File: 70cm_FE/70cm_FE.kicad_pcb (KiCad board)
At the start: 2 copper layers, 67 parts, among them J1 Conn_01x02, J2 U.FL, J3 U.FL, J4 Conn_01x02, J5 U.FL, Q1 BFU520W, U1 HT7533-1, U2 M68710L, U3 74HC14

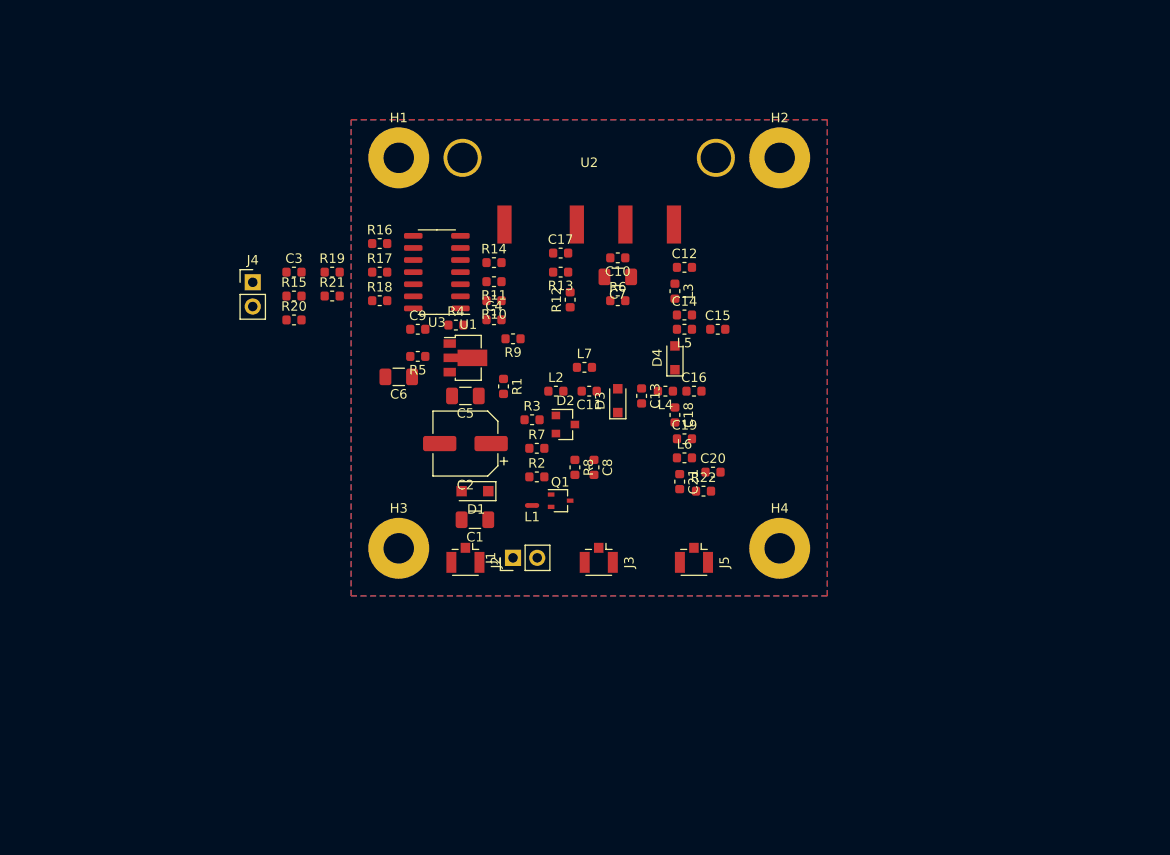
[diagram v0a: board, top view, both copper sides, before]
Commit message: Add some component values, add SAW footprint, change LNA transistor
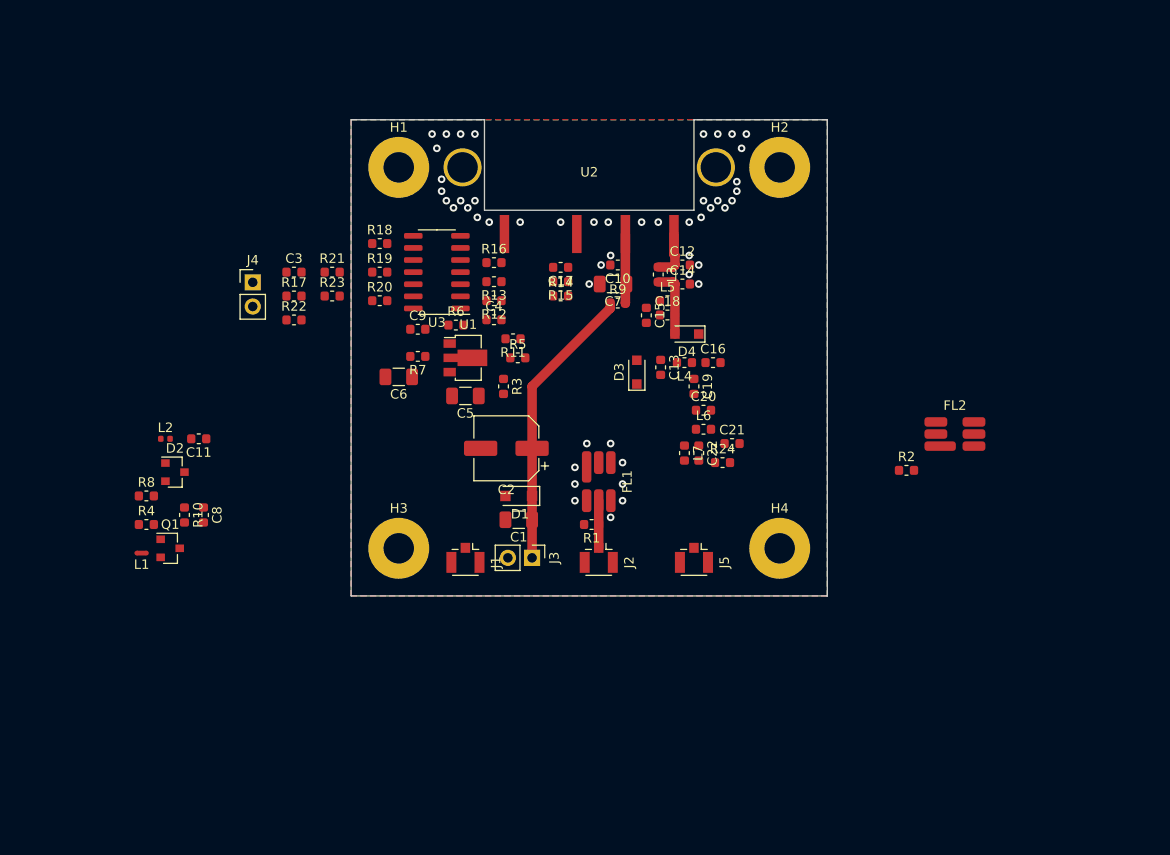
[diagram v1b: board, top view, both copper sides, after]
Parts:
- removed the J1 at (117.0, 96.0)
- removed the R7 at (119.5, 84.5)
- added C18: 2p2, Capacitor_SMD:C_0603_1608Metric, F.Cu at (133.2, 70.5)
- added FL1: AFS434S3, 70cm_FE:AFS434S3, F.Cu at (126.0, 88.0)
- added FL2: AFS434S3, 70cm_FE:AFS434S3, F.Cu at (163.4, 83.0)
- added J3: Conn_01x02, Connector_PinHeader_2.54mm:PinHeader_1x02_P2.54mm_Vertical, F.Cu at (119.0, 96.0)
- added R1: 100k, Resistor_SMD:R_0603_1608Metric, F.Cu at (125.2, 92.5)
- added R10: 2k2, Resistor_SMD:R_0603_1608Metric, F.Cu at (82.5, 91.5)
- added R4: 68, Resistor_SMD:R_0603_1608Metric, F.Cu at (78.5, 92.5)
- C11: value C -> 10p
- C13, C16: value C -> 5p6
- L2: value L -> 15n; footprint Inductor_SMD:L_0603_1608Metric -> Inductor_SMD:L_0402_1005Metric
- L4: value L -> 15n
- L5: value L -> 68n
- Q1: value BFU520W -> 2SC3356; footprint Package_TO_SOT_SMD:SOT-323_SC-70 -> Package_TO_SOT_SMD:SOT-23
- R2: value 68 -> 100k
- R24: renamed from R22; value R -> 100k
- R8: value 1k -> 4k7
- U2: footprint 70cm_pa:M68710L -> 70cm_FE:M68710L
- moved R8 45.1 mm to (78.5, 89.5), turned to 0 degrees
- moved C11 41.3 mm to (84.0, 83.5)
- moved C8 41.3 mm to (84.5, 91.5)
- moved D2 41.3 mm to (81.5, 87.0)
- moved L1 41.3 mm to (78.0, 95.5)
- moved L2 41.3 mm to (80.5, 83.5)
- moved Q1 41.3 mm to (81.0, 95.0)
- moved R2 38.8 mm to (158.3, 86.8)
- moved L7 13.8 mm to (135.0, 85.0), turned to 270 degrees
- moved C15 7.64 mm to (131.0, 70.5), turned to 270 degrees
- moved R5 6.67 mm to (117.5, 75.0)
- moved D1 4.63 mm to (117.6, 89.5)
- moved C1 4.60 mm to (117.6, 92.0)
- moved C2 4.33 mm to (116.3, 84.5)
- moved C13 3.61 mm to (132.5, 76.0)
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- renumbered C18 to C19, C19 to C20, C20 to C21, C21 to C22, J2 to J1, J3 to J2, R9 to R11, R10 to R12, R11 to R13, R12 to R14, R13 to R15, R14 to R16, R15 to R17, R16 to R18, R17 to R19, R18 to R20, R19 to R21, R20 to R22, R21 to R23, R1 to R3, R3 to R5, R4 to R6, R5 to R7, R6 to R9
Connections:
- C3 pad 2: /RX -> Net-(C3-Pad2)
- J1 pad 1: /PA_in -> /TX
- R2 pad 1: /LNA_EN -> Net-(C3-Pad2)
- R2 pad 2: Net-(C3-Pad1) -> GND
- R8 pad 1: Net-(C11-Pad2) -> Net-(Q1-Pad3)
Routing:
- net /V_in: track 0.00 -> 30.2 mm
- net /PA_VDD: track 0.00 -> 7.26 mm
- net Net-(C14-Pad1): track 0.00 -> 7.09 mm
- net /PA_out: track 0.00 -> 5.13 mm
- net /RX: track 0.00 -> 4.95 mm
- net GND: vias 0 -> 50
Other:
- board outline added: 50 x 50 mm

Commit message: Add driver stage and jumpers, clean up schematic
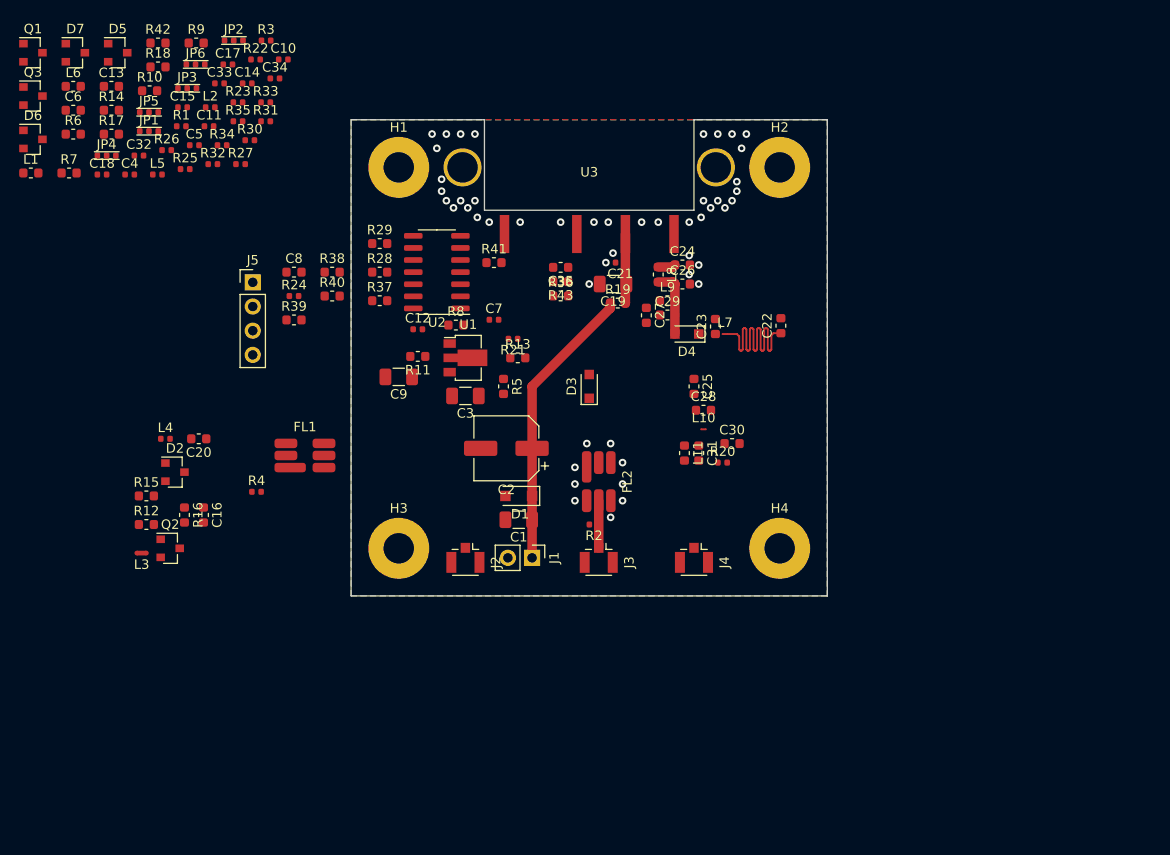
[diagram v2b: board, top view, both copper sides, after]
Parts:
- removed the C3 at (94.0, 66.0)
- removed the J4 at (89.7, 67.1)
- removed the R12 at (115.0, 69.0)
- removed the R13 at (115.0, 67.0)
- removed the R21 at (98.0, 66.0)
- added C10: 10p, Capacitor_SMD:C_0402_1005Metric, F.Cu at (92.9, 43.7)
- added C11: 1n, Capacitor_SMD:C_0402_1005Metric, F.Cu at (85.1, 50.7)
- added C13: 10p, Capacitor_SMD:C_0603_1608Metric, F.Cu at (74.8, 46.5)
- added C14: ?, Capacitor_SMD:C_0402_1005Metric, F.Cu at (89.1, 46.2)
- added C15: 1n, Capacitor_SMD:C_0402_1005Metric, F.Cu at (82.3, 48.7)
- added C17: 1n, Capacitor_SMD:C_0402_1005Metric, F.Cu at (87.1, 44.2)
- added C18: ?, Capacitor_SMD:C_0402_1005Metric, F.Cu at (73.8, 55.8)
- added C32: DNP, Capacitor_SMD:C_0402_1005Metric, F.Cu at (77.7, 53.8)
- added C33: DNP, Capacitor_SMD:C_0402_1005Metric, F.Cu at (86.2, 46.2)
- added C34: DNP, Capacitor_SMD:C_0402_1005Metric, F.Cu at (92.0, 45.7)
- added C4: 1n, Capacitor_SMD:C_0402_1005Metric, F.Cu at (76.8, 55.8)
- added C5: 1n, Capacitor_SMD:C_0402_1005Metric, F.Cu at (83.5, 52.7)
- added C6: 100p, Capacitor_SMD:C_0603_1608Metric, F.Cu at (70.8, 49.0)
- added C8: 100p, Capacitor_SMD:C_0603_1608Metric, F.Cu at (94.0, 66.0)
- added D5: BAV99, Package_TO_SOT_SMD:SOT-23, F.Cu at (75.5, 43.0)
- added D6: BAV99, Package_TO_SOT_SMD:SOT-23, F.Cu at (66.6, 52.1)
- added D7: BAV99, Package_TO_SOT_SMD:SOT-23, F.Cu at (71.0, 43.0)
- added J5: ~, Connector_PinHeader_2.54mm:PinHeader_1x04_P2.54mm_Vertical, F.Cu at (89.7, 67.1)
- added JP1: ~, 70cm_FE:Jumper-3_0402, F.Cu at (78.3, 51.2)
- added JP2: ~, 70cm_FE:Jumper-3_0402, F.Cu at (87.2, 41.7)
- added JP3: ~, 70cm_FE:Jumper-3_0402, F.Cu at (82.3, 46.7)
- added JP4: ~, 70cm_FE:Jumper-3_0402, F.Cu at (73.8, 53.8)
- added JP5: ~, 70cm_FE:Jumper-3_0402, F.Cu at (78.3, 49.2)
- added JP6: ~, 70cm_FE:Jumper-3_0402, F.Cu at (83.2, 44.2)
- added L1: 68n, Inductor_SMD:L_0603_1608Metric, F.Cu at (66.4, 55.6)
- added L2: 15n?, Inductor_SMD:L_0402_1005Metric, F.Cu at (85.2, 48.7)
- added L5: 15n?, Inductor_SMD:L_0402_1005Metric, F.Cu at (79.7, 55.8)
- added L6: 68n, Inductor_SMD:L_0603_1608Metric, F.Cu at (70.8, 46.5)
- added Q1: 2SC3356, Package_TO_SOT_SMD:SOT-23, F.Cu at (66.6, 43.0)
- added Q3: 2SC3356, Package_TO_SOT_SMD:SOT-23, F.Cu at (66.6, 47.5)
- added R1: 100k, Resistor_SMD:R_0402_1005Metric, F.Cu at (82.2, 50.7)
- added R10: 1k, Resistor_SMD:R_0603_1608Metric, F.Cu at (78.8, 47.0)
- added R14: 100, Resistor_SMD:R_0603_1608Metric, F.Cu at (74.8, 49.0)
- added R18: 10, Resistor_SMD:R_0603_1608Metric, F.Cu at (79.7, 44.5)
- added R24: 100k, Resistor_SMD:R_0402_1005Metric, F.Cu at (94.0, 68.5)
- added R25: 0, Resistor_SMD:R_0402_1005Metric, F.Cu at (82.6, 55.2)
- added R26: 0, Resistor_SMD:R_0402_1005Metric, F.Cu at (80.6, 53.2)
- added R27: 0, Resistor_SMD:R_0402_1005Metric, F.Cu at (88.4, 54.7)
- added R3: 100k, Resistor_SMD:R_0402_1005Metric, F.Cu at (91.1, 41.7)
- added R30: DNP, Resistor_SMD:R_0402_1005Metric, F.Cu at (89.4, 52.1)
- added R31: DNP, Resistor_SMD:R_0402_1005Metric, F.Cu at (91.0, 50.2)
- added R32: DNP, Resistor_SMD:R_0402_1005Metric, F.Cu at (85.5, 54.7)
- added R33: DNP, Resistor_SMD:R_0402_1005Metric, F.Cu at (91.0, 48.2)
- added R34: DNP, Resistor_SMD:R_0402_1005Metric, F.Cu at (86.5, 52.7)
- added R35: DNP, Resistor_SMD:R_0402_1005Metric, F.Cu at (88.1, 50.2)
- added R38: DNP, Resistor_SMD:R_0603_1608Metric, F.Cu at (98.0, 66.0)
- added R39: 0, Resistor_SMD:R_0603_1608Metric, F.Cu at (94.0, 71.0)
- added R40: DNP, Resistor_SMD:R_0603_1608Metric, F.Cu at (98.0, 68.5)
- added R42: 100, Resistor_SMD:R_0603_1608Metric, F.Cu at (79.7, 41.9)
- added R6: 1, Resistor_SMD:R_0603_1608Metric, F.Cu at (70.8, 51.5)
- added R7: 4k7, Resistor_SMD:R_0603_1608Metric, F.Cu at (70.4, 55.6)
- added R9: 1k, Resistor_SMD:R_0603_1608Metric, F.Cu at (83.7, 41.9)
- C12: renamed from C9; footprint Capacitor_SMD:C_0603_1608Metric -> Capacitor_SMD:C_0402_1005Metric
- C21: renamed from C10; footprint Capacitor_SMD:C_0603_1608Metric -> Capacitor_SMD:C_0402_1005Metric
- C7: renamed from C4; value 100n -> 1n; footprint Capacitor_SMD:C_0603_1608Metric -> Capacitor_SMD:C_0402_1005Metric
- J1: renamed from J3; value Conn_01x02 -> ~
- L10: renamed from L6; footprint Inductor_SMD:L_0603_1608Metric -> 70cm_FE:NetTie-2_SMD_Pad0.2mm
- L7: renamed from L4; footprint Inductor_SMD:L_0603_1608Metric -> 70cm_FE:NetTie-2_SMD_Pad0.2mm
- R17: value 100k -> 1
- R2: renamed from R1; footprint Resistor_SMD:R_0603_1608Metric -> Resistor_SMD:R_0402_1005Metric
- R20: renamed from R24; footprint Resistor_SMD:R_0603_1608Metric -> Resistor_SMD:R_0402_1005Metric
- R21: renamed from R11; footprint Resistor_SMD:R_0603_1608Metric -> Resistor_SMD:R_0402_1005Metric
- R22: footprint Resistor_SMD:R_0603_1608Metric -> Resistor_SMD:R_0402_1005Metric
- R23: value DNP -> 0; footprint Resistor_SMD:R_0603_1608Metric -> Resistor_SMD:R_0402_1005Metric
- R28: renamed from R19; value 1k -> 100
- R29: renamed from R18; value 0 -> 100k
- R4: renamed from R2; footprint Resistor_SMD:R_0603_1608Metric -> Resistor_SMD:R_0402_1005Metric
- moved FL1 68.3 mm to (95.2, 85.2)
- moved R4 68.3 mm to (90.1, 89.1)
- moved R22 27.6 mm to (90.0, 43.7)
- moved R17 25.6 mm to (74.8, 51.5)
- moved R23 22.6 mm to (88.1, 48.2)
- moved C22 13.4 mm to (145.1, 71.6), turned to 90 degrees
- moved D3 5.22 mm to (125.0, 78.0)
- moved L7 5.20 mm to (139.2, 72.5), turned to 0 degrees
- moved C23 3.80 mm to (138.2, 71.7), turned to 90 degrees
- moved C21 0.35 mm to (128.2, 65.0)
- moved R2 0.25 mm to (125.5, 92.5)
- renumbered C8 to C16, C7 to C19, C11 to C20, C13 to C22, C16 to C23, C12 to C24, C19 to C25, C14 to C26, C15 to C27, C20 to C28, C18 to C29, C5 to C3, C21 to C30, C22 to C31, C17 to C35, C6 to C9, FL2 to FL1, FL1 to FL2, J1 to J2, J2 to J3, J5 to J4, L7 to L11, L1 to L3, L2 to L4, L3 to L8, L5 to L9, Q1 to Q2, R7 to R11, R4 to R12, R5 to R13, R8 to R15, R10 to R16, R9 to R19, R14 to R36, R20 to R37, R16 to R41, R15 to R43, R3 to R5, R6 to R8, U3 to U2, U2 to U3
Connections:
- net Net-(C15-Pad1) renamed /PIN_bias
- net Net-(C3-Pad2) renamed /RXSAW_IN
- C3 pad 1: Net-(C5-Pad1) -> Net-(C3-Pad1)
- C7 pad 1: /LNA_EN -> Net-(C7-Pad1)
- FL1 pad 2: Net-(FL2-Pad2) -> /TXSAW_in
- FL1 pad 5: Net-(FL2-Pad5) -> /TXSAW_out
- FL2 pad 5: /RX -> /RXSAW_OUT
- R12 pad 1: /LNA_EN -> Net-(C7-Pad1)
- R17 pad 1: /TX_EN_IN -> /VDD
- R17 pad 2: GND -> Net-(C17-Pad1)
- R19 pad 1: /V_in -> /PA_VDD
- R19 pad 2: /PA_VDD -> /V_in
- R2 pad 1: /RX -> /RXSAW_OUT
- R21 pad 1: /TX_EN -> /TX_ON
- R21 pad 2: Net-(R11-Pad2) -> Net-(R21-Pad2)
- R22 pad 1: Net-(R22-Pad1) -> /TX_ON
- R22 pad 2: /TX_EN -> Net-(R22-Pad2)
- R23 pad 1: Net-(R22-Pad1) -> /~TX_ON~
- R23 pad 2: /~TX_EN~ -> Net-(R23-Pad2)
- R28 pad 1: /TX_EN_IN -> /TX_ON_IN
- R29 pad 1: GND -> /VDD
- R36 pad 1: Net-(R14-Pad1) -> /PA_EN
- R37 pad 2: /~TX_EN~ -> /~TX_ON~
- R41 pad 1: /PIN_EN -> Net-(R41-Pad1)
- R5 pad 1: Net-(C5-Pad1) -> /V_in
- R5 pad 2: /V_in -> Net-(C3-Pad1)
- U1 pad 2: Net-(C5-Pad1) -> Net-(C3-Pad1)
- U2 pad 1: Net-(R11-Pad2) -> Net-(C32-Pad1)
- U2 pad 12: Net-(R22-Pad1) -> Net-(R39-Pad1)
- U2 pad 4: Net-(R14-Pad1) -> Net-(R41-Pad1)
- U2 pad 6: /PIN_EN -> /PA_EN
- U2 pad 8: Net-(U3-Pad8) -> /TX_detect
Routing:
- net Net-(C20-Pad1): track 0.00 -> 26.6 mm
- net /PA_out: track 5.13 -> 1.84 mm

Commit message: Add RF detector, more layout
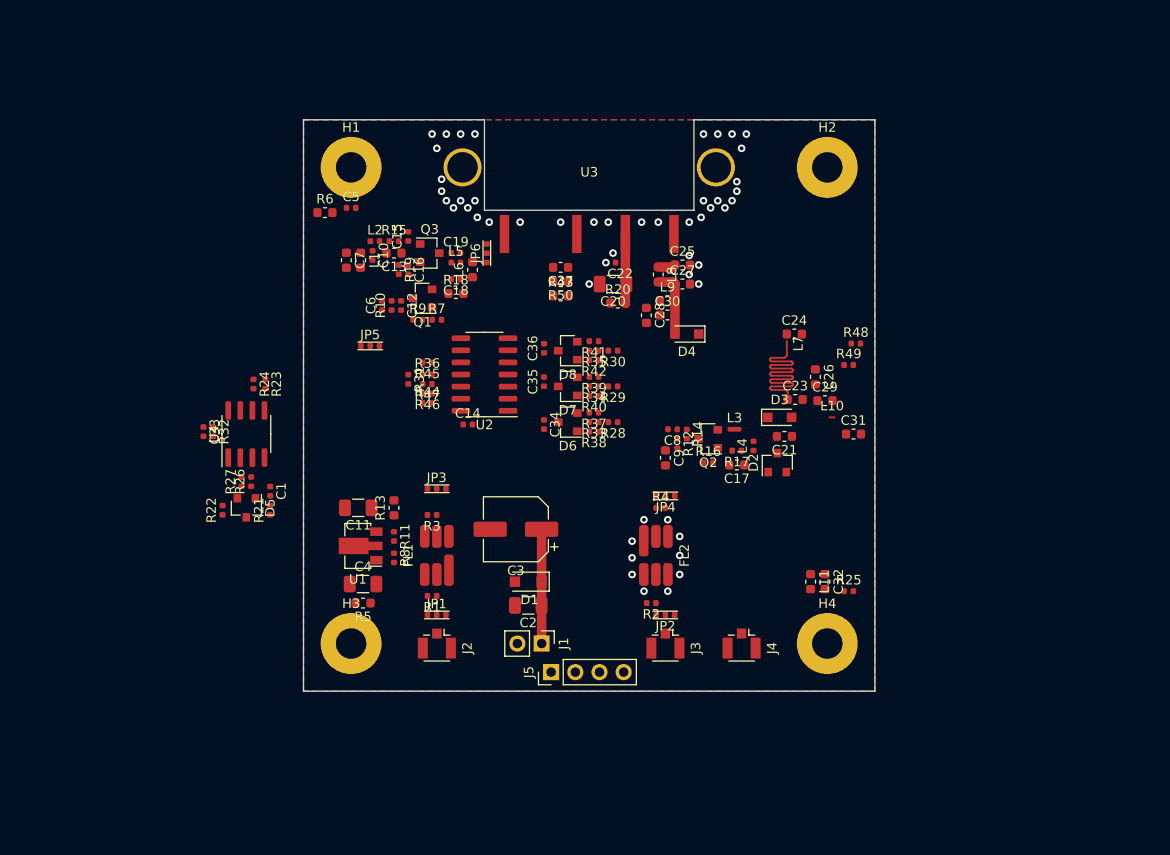
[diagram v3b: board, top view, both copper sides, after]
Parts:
- removed the C3 at (112.0, 79.0)
- removed the C9 at (105.0, 77.0)
- added C1: 1p, Capacitor_SMD:C_0402_1005Metric, F.Cu at (91.5, 89.0)
- added C11: 10u, Capacitor_SMD:C_1206_3216Metric, F.Cu at (100.8, 90.8)
- added C33: 10p, Capacitor_SMD:C_0402_1005Metric, F.Cu at (84.5, 82.8)
- added C4: 10u, Capacitor_SMD:C_1206_3216Metric, F.Cu at (101.2, 98.8)
- added D5: BAT54C, Package_TO_SOT_SMD:SOT-23, F.Cu at (89.0, 90.8)
- added R13: 1, Resistor_SMD:R_0603_1608Metric, F.Cu at (104.5, 90.8)
- added R21: 100k, Resistor_SMD:R_0402_1005Metric, F.Cu at (91.5, 91.0)
- added R22: 220k, Resistor_SMD:R_0402_1005Metric, F.Cu at (86.5, 91.0)
- added R23: 100k, Resistor_SMD:R_0402_1005Metric, F.Cu at (91.0, 77.8)
- added R24: 1k, Resistor_SMD:R_0402_1005Metric, F.Cu at (89.8, 77.8)
- added R26: 1k, Resistor_SMD:R_0402_1005Metric, F.Cu at (89.5, 88.0)
- added R27: 1k, Resistor_SMD:R_0402_1005Metric, F.Cu at (88.5, 88.0)
- added U4: LM393, Package_SO:SOIC-8_3.9x4.9mm_P1.27mm, F.Cu at (89.0, 83.0)
- R10, R7, R8, R9: footprint Resistor_SMD:R_0603_1608Metric -> Resistor_SMD:R_0402_1005Metric
- R11: value 1 -> DNP; footprint Resistor_SMD:R_0603_1608Metric -> Resistor_SMD:R_0402_1005Metric
- R12: renamed from R13; footprint Resistor_SMD:R_0603_1608Metric -> Resistor_SMD:R_0402_1005Metric
- R14: renamed from R12; footprint Resistor_SMD:R_0603_1608Metric -> Resistor_SMD:R_0402_1005Metric
- R15: renamed from R14; footprint Resistor_SMD:R_0603_1608Metric -> Resistor_SMD:R_0402_1005Metric
- R16: renamed from R15; footprint Resistor_SMD:R_0603_1608Metric -> Resistor_SMD:R_0402_1005Metric
- R17: renamed from R16; footprint Resistor_SMD:R_0603_1608Metric -> Resistor_SMD:R_0402_1005Metric
- R19: renamed from R18; footprint Resistor_SMD:R_0603_1608Metric -> Resistor_SMD:R_0402_1005Metric
- R32: renamed from R29; footprint Resistor_SMD:R_0603_1608Metric -> Resistor_SMD:R_0402_1005Metric
- R36: renamed from R28; footprint Resistor_SMD:R_0603_1608Metric -> Resistor_SMD:R_0402_1005Metric
- R44: renamed from R37; footprint Resistor_SMD:R_0603_1608Metric -> Resistor_SMD:R_0402_1005Metric
- R45: renamed from R38; footprint Resistor_SMD:R_0603_1608Metric -> Resistor_SMD:R_0402_1005Metric
- R46: renamed from R39; footprint Resistor_SMD:R_0603_1608Metric -> Resistor_SMD:R_0402_1005Metric
- R47: renamed from R40; footprint Resistor_SMD:R_0603_1608Metric -> Resistor_SMD:R_0402_1005Metric
- R48: renamed from R41; footprint Resistor_SMD:R_0603_1608Metric -> Resistor_SMD:R_0402_1005Metric
- R49: renamed from R42; footprint Resistor_SMD:R_0603_1608Metric -> Resistor_SMD:R_0402_1005Metric
- moved R49 80.0 mm to (152.2, 75.8)
- moved JP2 76.0 mm to (133.5, 102.0), turned to 180 degrees
- moved JP4 69.5 mm to (133.5, 89.5), turned to 180 degrees
- moved L3 63.6 mm to (140.2, 82.5), turned to 0 degrees
- moved D2 63.3 mm to (144.8, 86.0), turned to 90 degrees
- moved D7 61.9 mm to (122.8, 78.0), turned to 180 degrees
- moved L4 61.8 mm to (142.2, 84.2), turned to 90 degrees
- moved C21 61.5 mm to (145.5, 83.2)
- moved D6 61.1 mm to (122.8, 81.8), turned to 180 degrees
- moved D8 60.4 mm to (122.8, 74.2), turned to 180 degrees
- moved JP1 59.1 mm to (108.5, 102.0)
- moved R16 59.1 mm to (137.5, 86.0)
- moved R17 58.4 mm to (140.5, 84.8), turned to 180 degrees
- moved Q2 57.7 mm to (137.5, 83.5), turned to 180 degrees
- moved R14 57.5 mm to (135.2, 83.0), turned to 270 degrees
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- renumbered C11 to C12, C12 to C14, C14 to C15, C15 to C16, C16 to C17, C17 to C18, C18 to C19, C1 to C2, C19 to C20, C20 to C21, C21 to C22, C22 to C23, C23 to C24, C24 to C25, C25 to C26, C26 to C27, C27 to C28, C28 to C29, C2 to C3, C29 to C30, C30 to C31, C31 to C32, C32 to C34, C33 to C35, C34 to C36, C35 to C37, C4 to C5, C5 to C6, C6 to C7, C7 to C8, C8 to C9, D5 to D6, D6 to D7, D7 to D8, R17 to R18, R19 to R20, R20 to R25, R21 to R28, R22 to R29, R23 to R30, R24 to R31, R25 to R33, R26 to R34, R27 to R35, R30 to R37, R31 to R38, R32 to R39, R33 to R40, R34 to R41, R35 to R42, R36 to R43, R43 to R50
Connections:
- net Net-(C13-Pad1) renamed /DRV_B
- net Net-(C15-Pad1) renamed /DRV_E
- net Net-(C16-Pad2) renamed /LNA_B
- net Net-(C20-Pad1) renamed /PIN_RXRF
- net Net-(C23-Pad1) renamed /PIN_COMRF
- net Net-(C26-Pad1) renamed /PIN_TXRF
- net Net-(C32-Pad1) renamed /~LNA_EN_SEQ~
- net Net-(C33-Pad1) renamed /~PIN_EN_SEQ~
- net Net-(C34-Pad1) renamed /~PA_EN_SEQ~
- net Net-(C7-Pad1) renamed /LNA_VCC
- net Net-(L3-Pad1) renamed /LNA_E
- net Net-(R21-Pad2) renamed /~LNA_EN_IN~
- net Net-(R22-Pad2) renamed /~PIN_EN_IN~
- net Net-(R23-Pad2) renamed /~PA_EN_IN~
- net Net-(R29-Pad2) renamed /DET_timing
- C19 pad 1: Net-(C18-Pad1) (its old number) -> /DRV_C
- C9 pad 1: Net-(C8-Pad1) -> Net-(C9-Pad1)
- JP5 pad 1: /DRV_bypass -> /DRV_IN
- JP5 pad 3: /DRV_IN -> /DRV_bypass
- L5 pad 1: Net-(C18-Pad1) (its old number) -> /DRV_C
- Q2 pad 3: Net-(Q2-Pad3) -> /LNA_C
- Q3 pad 3: Net-(C18-Pad1) (its old number) -> /DRV_C
- R11 pad 2: Net-(C9-Pad1) -> Net-(R11-Pad2)
- R12 pad 1: Net-(Q2-Pad3) -> /LNA_C
- R12 pad 2: Net-(C8-Pad1) -> Net-(C9-Pad1)
- R14 pad 2: Net-(C8-Pad1) -> /LNA_C
- R16 pad 1: Net-(Q2-Pad3) -> /LNA_C
- R8 pad 1: Net-(R8-Pad1) -> Net-(R11-Pad2)
- U1 pad 1: Net-(R8-Pad1) -> Net-(R11-Pad2)
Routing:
- net /V_in: track 30.2 -> 11.5 mm
- net /RX: track 4.95 -> 0.00 mm
- net GND: vias 50 -> 51
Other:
- board size 50 x 50 mm -> 60 x 60 mm
